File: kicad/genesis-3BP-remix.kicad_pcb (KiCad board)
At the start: 2 copper layers, 29 x 38.5 mm, 91 parts, among them CON1 MD-90SM, J1 S, J10 XL, J11 CL, J12 YL, J2 R, J3 G, J4 B, J5 VS, J6 YR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

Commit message: Update cap pad change
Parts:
- C21, C22, C8: footprint Capacitor_Tantalum_SMD:CP_EIA-3528-21_Kemet-B -> Capacitor_Tantalum_SMD:CP_EIA-3528-15_AVX-H

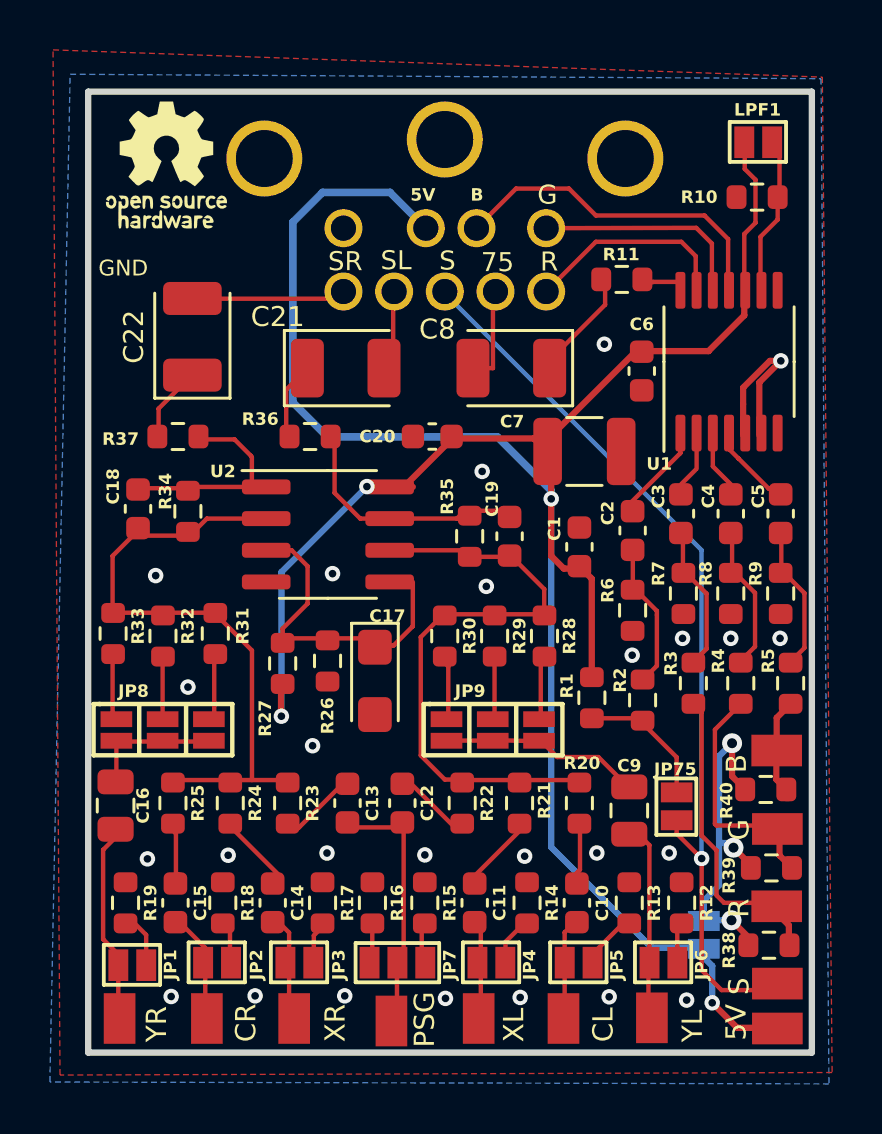
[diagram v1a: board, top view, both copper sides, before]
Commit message: Update silkscreen placement
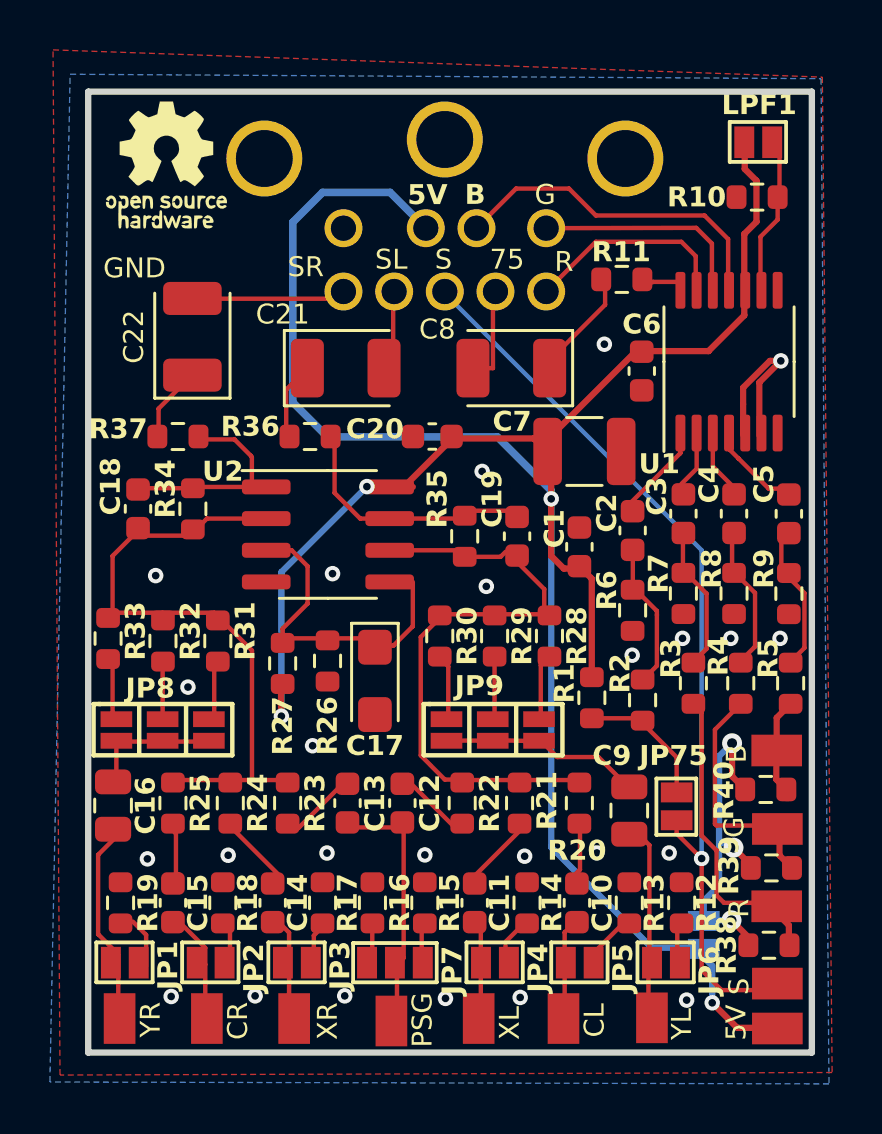
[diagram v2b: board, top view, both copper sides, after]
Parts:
- U2: value TLV9062xD -> TL972IDR
- moved C5 0.33 mm to (151.3, 98.1)
- moved R9 0.33 mm to (151.3, 101.3)
- moved JP1 0.32 mm to (125.0, 116.1)
- moved R31 0.32 mm to (128.4, 103.2)
- moved C19 0.30 mm to (140.4, 99.0)
- moved R33 0.28 mm to (124.0, 103.1)
- moved JP2 0.26 mm to (128.4, 116.1)
- moved R34 0.22 mm to (127.4, 97.9)
- moved R19 0.20 mm to (124.5, 113.7)
- moved R32 0.20 mm to (126.2, 103.2)
- moved R28 0.20 mm to (141.7, 103.0)
- moved R30 0.20 mm to (137.3, 103.0)
- moved R35 0.20 mm to (138.3, 99.0)
- moved JP4 0.14 mm to (139.8, 116.1)
- moved C4 0.13 mm to (149.1, 98.1)
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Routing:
- net GND: vias 26 -> 25
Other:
- board text added: "Board design by tianfeng32, zaxour, rhombic-drive"
- board text removed: "Board design by"
